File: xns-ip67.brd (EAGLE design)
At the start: 65.3 x 129.3 mm, 119 parts, among them J1 DCJ0202

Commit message: Rev 0
First Version without routing
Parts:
- removed SV1: (no value), con-lstb:MA03-1
- added 5.5V, PAD115, PAD116: WIREPAD1,6/0,9, wirepad:1,6/0,9
- added JP1, JP10, JP11, JP12, JP13, JP14, JP15, JP16, JP17, JP18, JP19, JP2, JP20, JP21, JP22, JP23, JP24, JP25, JP26, JP27, JP28, JP29, JP3, JP30, JP35, JP36, JP4, JP5, JP6, JP7, JP8, JP9: (no value), adafruit:1X08-CLEANBIG
- added JP31, JP32, JP33, JP34: (no value), microbuilder:1X12_ROUND
- added PROG: (no value), con-lstb:MA03-1
- added U1: (no value), SparkFun-PowerIC:SOT23-5
- added X2: (no value), microbuilder:4UCONN_20329
- moved PAD16 80.2 mm to (72.4, 21.6)
- moved PAD22 78.5 mm to (69.8, 29.2)
- moved PAD20 78.5 mm to (69.8, 31.8)
- moved PAD19 78.5 mm to (72.4, 31.8)
- moved PAD18 78.5 mm to (72.4, 29.2)
- moved PAD17 78.5 mm to (72.4, 26.7)
- moved PAD9 78.4 mm to (69.8, 47.0)
- moved PAD7 78.4 mm to (69.8, 44.5)
- moved PAD8 78.4 mm to (69.8, 34.3)
- moved PAD11 78.4 mm to (69.8, 41.9)
- moved PAD12 78.4 mm to (69.8, 39.4)
- moved PAD10 78.4 mm to (69.8, 36.8)
- moved PAD6 78.4 mm to (72.4, 47.0)
- moved PAD5 78.4 mm to (72.4, 44.5)
- moved PAD4 78.4 mm to (72.4, 41.9)
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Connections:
- new net N$23: JP3.1, JP3.2, JP3.3, JP3.4, JP3.5, JP3.6, JP3.7, JP3.8
- new net N$24: JP4.1, JP4.2, JP4.3, JP4.4, JP4.5, JP4.6, JP4.7, JP4.8
- new net N$25: JP5.1, JP5.2, JP5.3, JP5.4, JP5.5, JP5.6, JP5.7, JP5.8
- new net N$26: JP6.1, JP6.2, JP6.3, JP6.4, JP6.5, JP6.6, JP6.7, JP6.8
- new net N$27: JP7.1, JP7.2, JP7.3, JP7.4, JP7.5, JP7.6, JP7.7, JP7.8
- new net N$28: JP8.1, JP8.2, JP8.3, JP8.4, JP8.5, JP8.6, JP8.7, JP8.8
- new net N$29: JP9.1, JP9.2, JP9.3, JP9.4, JP9.5, JP9.6, JP9.7, JP9.8
- new net N$30: JP10.1, JP10.2, JP10.3, JP10.4, JP10.5, JP10.6, JP10.7, JP10.8
- new net N$31: JP11.1, JP11.2, JP11.3, JP11.4, JP11.5, JP11.6, JP11.7, JP11.8
- new net N$32: JP12.1, JP12.2, JP12.3, JP12.4, JP12.5, JP12.6, JP12.7, JP12.8
- new net N$33: JP13.1, JP13.2, JP13.3, JP13.4, JP13.5, JP13.6, JP13.7, JP13.8
- new net N$34: JP14.1, JP14.2, JP14.3, JP14.4, JP14.5, JP14.6, JP14.7, JP14.8
- new net N$35: JP15.1, JP15.2, JP15.3, JP15.4, JP15.5, JP15.6, JP15.7, JP15.8
- new net N$36: JP30.1, JP30.2, JP30.3, JP30.4, JP30.5, JP30.6, JP30.7, JP30.8
- new net N$37: JP29.1, JP29.2, JP29.3, JP29.4, JP29.5, JP29.6, JP29.7, JP29.8
- new net N$38: JP28.1, JP28.2, JP28.3, JP28.4, JP28.5, JP28.6, JP28.7, JP28.8
- new net N$39: JP27.1, JP27.2, JP27.3, JP27.4, JP27.5, JP27.6, JP27.7, JP27.8
- new net N$40: JP26.1, JP26.2, JP26.3, JP26.4, JP26.5, JP26.6, JP26.7, JP26.8
- new net N$41: JP25.1, JP25.2, JP25.3, JP25.4, JP25.5, JP25.6, JP25.7, JP25.8
- new net N$42: JP24.1, JP24.2, JP24.3, JP24.4, JP24.5, JP24.6, JP24.7, JP24.8
- new net N$43: JP22.1, JP22.2, JP22.3, JP22.4, JP22.5, JP22.6, JP22.7, JP22.8
- new net N$44: JP21.1, JP21.2, JP21.3, JP21.4, JP21.5, JP21.6, JP21.7, JP21.8
- new net N$45: JP20.1, JP20.2, JP20.3, JP20.4, JP20.5, JP20.6, JP20.7, JP20.8
- new net N$46: JP19.1, JP19.2, JP19.3, JP19.4, JP19.5, JP19.6, JP19.7, JP19.8
- new net N$47: JP18.1, JP18.2, JP18.3, JP18.4, JP18.5, JP18.6, JP18.7, JP18.8
- new net N$48: JP17.1, JP17.2, JP17.3, JP17.4, JP17.5, JP17.6, JP17.7, JP17.8
- new net N$49: JP16.1, JP16.2, JP16.3, JP16.4, JP16.5, JP16.6, JP16.7, JP16.8
- new net N$50: JP35.1, JP35.2, JP35.3, JP35.4, JP35.5, JP35.6, JP35.7, JP35.8
- new net N$51: JP36.1, JP36.2, JP36.3, JP36.4, JP36.5, JP36.6, JP36.7, JP36.8
- net GND: now also JP31.1, JP31.10, JP31.11, JP31.12, JP31.2, JP31.3, JP31.4, JP31.5, JP31.6, JP31.7, JP31.8, JP31.9, JP32.1, JP32.10, JP32.11, JP32.12, JP32.2, JP32.3, JP32.4, JP32.5, JP32.6, JP32.7, JP32.8, JP32.9, MDL1.9, PAD107.1, PAD108.1, PAD109.1, PAD110.1, PAD111.1, PAD25.1, PAD26.1, PAD39.1, PAD40.1, PROG.1, U1.2, X1.2, X2.BASE@1, X2.BASE@2, X2.GND, X2.SPRT@1, X2.SPRT@2, X2.SPRT@3, X2.SPRT@4
- net N$14: now also MDL1.22
- net N$15: now also MDL1.10
- net N$16: now also MDL1.11
- net N$17: now also MDL1.12
- net N$18: now also MDL1.13
- net N$19: now also MDL1.14
- net N$20: now also MDL1.16, PROG.3; no longer PAD103.1, PAD104.1, PAD105.1, PAD106.1
- net N$21: now also JP1.1, JP1.2, JP1.3, JP1.4, JP1.5, JP1.6, JP1.7, JP1.8; no longer PAD107.1, PAD108.1, PAD109.1, PAD110.1
- net N$22: now also JP2.1, JP2.2, JP2.3, JP2.4, JP2.5, JP2.6, JP2.7, JP2.8; no longer PAD111.1, PAD112.1, PAD113.1, PAD114.1
- net N$4: now also MDL1.15, PROG.2; no longer MDL1.8, PAD39.1, PAD40.1, PAD41.1, PAD42.1
- net VCC: now also 5.5V.1, U1.1, U1.3, X1.1, X2.VBUS
- net VDD: now also JP33.1, JP33.10, JP33.11, JP33.12, JP33.2, JP33.3, JP33.4, JP33.5, JP33.6, JP33.7, JP33.8, JP33.9, JP34.1, JP34.10, JP34.11, JP34.12, JP34.2, JP34.3, JP34.4, JP34.5, JP34.6, JP34.7, JP34.8, JP34.9, MDL1.8, PAD103.1, PAD104.1, PAD105.1, PAD106.1, PAD112.1, PAD113.1, PAD114.1, PAD115.1, PAD116.1, PAD41.1, PAD42.1, U1.5; no longer PAD25.1, PAD26.1
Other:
- board text added: "3.3V"
- board text added: "GND"
- board text added: "RX"
- board text added: "TX"

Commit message: Rev 0 Autoroute
Rev 0 with Autoroute
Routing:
- net VDD: track 0.00 -> 277.9 mm, vias 0 -> 1
- net VCC: track 0.00 -> 68.2 mm
- net N$12: track 0.00 -> 21.8 mm
- net N$1: track 0.00 -> 21.5 mm
- net N$51: track 0.00 -> 19.7 mm
- net N$47: track 0.00 -> 19.7 mm
- net N$44: track 0.00 -> 19.7 mm
- net N$39: track 0.00 -> 19.7 mm
- net N$36: track 0.00 -> 19.7 mm
- net N$50: track 0.00 -> 19.7 mm
- net N$33: track 0.00 -> 19.7 mm
- net N$30: track 0.00 -> 19.7 mm
- net N$24: track 0.00 -> 19.7 mm
- net N$21: track 0.00 -> 19.7 mm
- net N$42: track 0.00 -> 19.7 mm
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- added copper zone on layer 1, net GND
- added copper zone on layer 16, net GND
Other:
- board text added: "xns-ip67-rev-0"
- board text added: "xnsense.no"

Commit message: New route
reroute
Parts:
- moved JP31 1.27 mm to (15.9, 86.4)
- moved JP34 1.27 mm to (18.4, 86.4)
- moved JP1 0.63 mm to (31.8, 100.3)
- moved JP10 0.63 mm to (31.8, 77.5)
- moved JP11 0.63 mm to (31.8, 74.9)
- moved JP12 0.63 mm to (31.8, 72.4)
- moved JP13 0.63 mm to (31.8, 69.8)
- moved JP14 0.63 mm to (31.8, 67.3)
- moved JP15 0.63 mm to (31.8, 64.8)
- moved JP16 0.63 mm to (54.6, 64.8)
- moved JP17 0.63 mm to (54.6, 67.3)
- moved JP18 0.63 mm to (54.6, 69.8)
- moved JP19 0.63 mm to (54.6, 72.4)
- moved JP2 0.63 mm to (31.8, 97.8)
- moved JP20 0.63 mm to (54.6, 74.9)
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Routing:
- net VDD: track 277.9 -> 271.4 mm
- net VCC: track 68.2 -> 68.9 mm

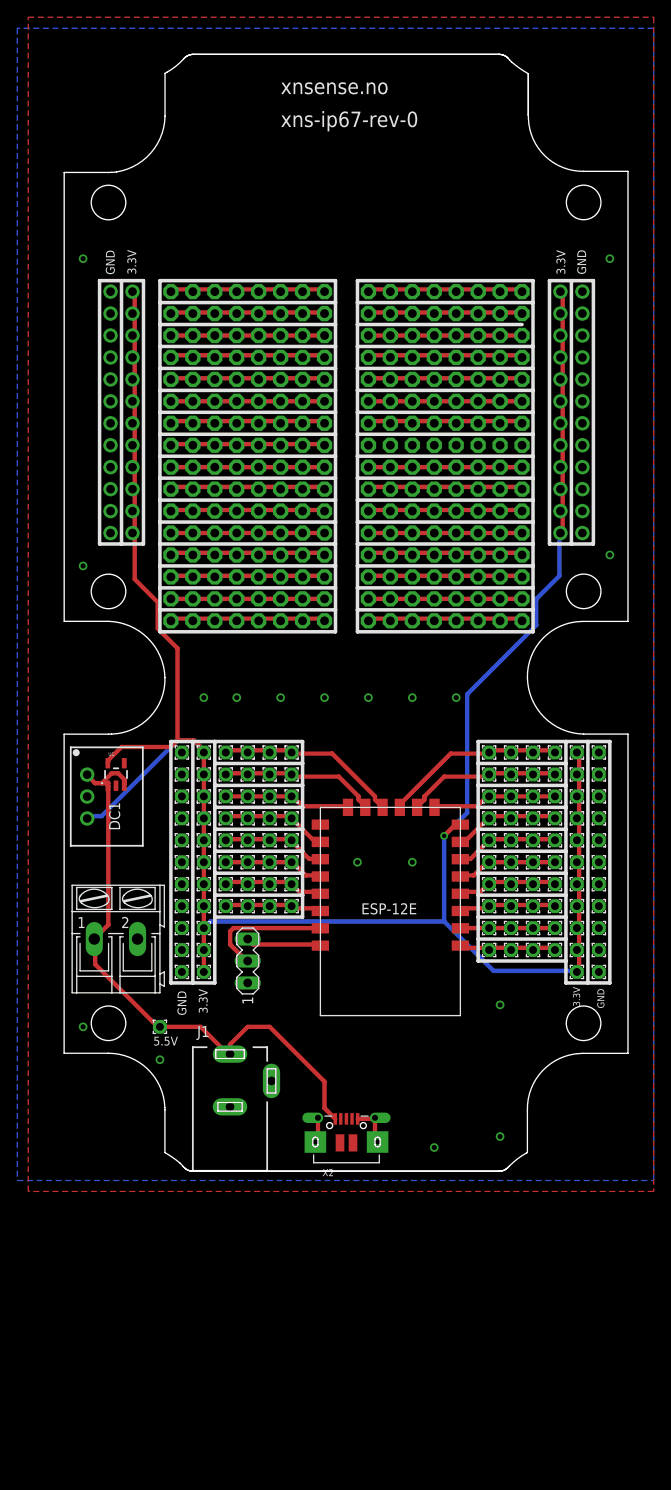
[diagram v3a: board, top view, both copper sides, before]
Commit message: Updated design
Added more wire pads on side of ESP
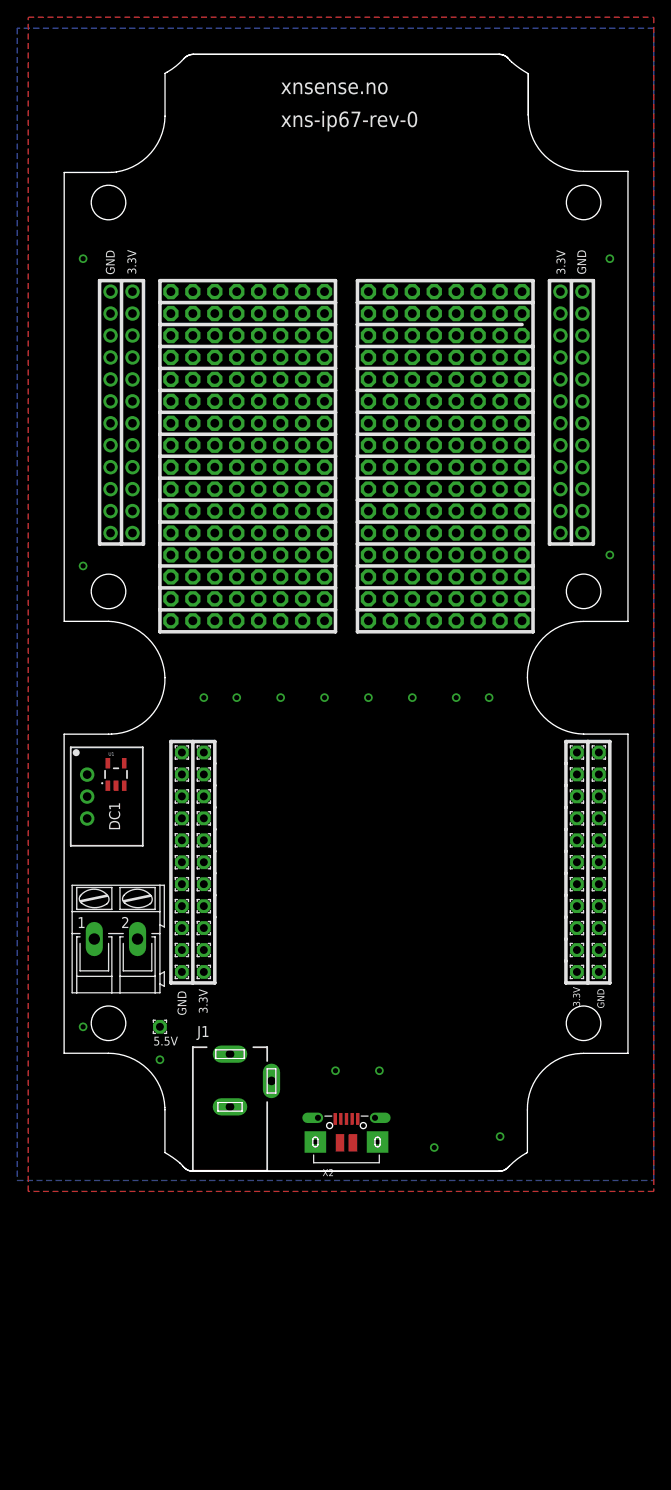
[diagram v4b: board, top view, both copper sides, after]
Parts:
- removed MDL1: (no value), ESP8266-ESP12E:ESP8266-ESP12E
- removed PAD100, PAD101, PAD102, PAD27, PAD28, PAD29, PAD30, PAD31, PAD32, PAD33, PAD34, PAD35, PAD36, PAD37, PAD38, PAD43, PAD44, PAD45, PAD46, PAD47, PAD48, PAD49, PAD50, PAD51, PAD52, PAD53, PAD54, PAD55, PAD56, PAD57, PAD58, PAD59, PAD60, PAD61, PAD62, PAD63, PAD64, PAD65, PAD66, PAD67, PAD68, PAD69, PAD70, PAD71, PAD72, PAD73, PAD74, PAD75, PAD76, PAD77, PAD78, PAD79, PAD80, PAD81, PAD82, PAD83, PAD84, PAD85, PAD86, PAD87, PAD88, PAD89, PAD90, PAD91, PAD92, PAD93, PAD94, PAD95, PAD96, PAD97, PAD98, PAD99: WIREPAD1,6/0,9, wirepad:1,6/0,9
- removed PROG: (no value), con-lstb:MA03-1
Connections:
- removed net N$1: MDL1.19, PAD27.1, PAD28.1, PAD29.1, PAD30.1
- removed net N$10: MDL1.2, PAD63.1, PAD64.1, PAD65.1, PAD66.1
- removed net N$11: MDL1.1, PAD67.1, PAD68.1, PAD69.1, PAD70.1
- removed net N$12: MDL1.20, PAD71.1, PAD72.1, PAD73.1, PAD74.1
- removed net N$13: MDL1.21, PAD75.1, PAD76.1, PAD77.1, PAD78.1
- removed net N$14: MDL1.22, PAD79.1, PAD80.1, PAD81.1, PAD82.1
- removed net N$15: MDL1.10, PAD83.1, PAD84.1, PAD85.1, PAD86.1
- removed net N$16: MDL1.11, PAD87.1, PAD88.1, PAD89.1, PAD90.1
- removed net N$17: MDL1.12, PAD91.1, PAD92.1, PAD93.1, PAD94.1
- removed net N$18: MDL1.13, PAD95.1, PAD96.1, PAD97.1, PAD98.1
- removed net N$19: MDL1.14, PAD100.1, PAD101.1, PAD102.1, PAD99.1
- removed net N$2: MDL1.18, PAD31.1, PAD32.1, PAD33.1, PAD34.1
- removed net N$20: MDL1.16, PROG.3
- removed net N$3: MDL1.17, PAD35.1, PAD36.1, PAD37.1, PAD38.1
- removed net N$4: MDL1.15, PROG.2
- removed net N$5: MDL1.7, PAD43.1, PAD44.1, PAD45.1, PAD46.1
- removed net N$6: MDL1.6, PAD47.1, PAD48.1, PAD49.1, PAD50.1
- removed net N$7: MDL1.5, PAD51.1, PAD52.1, PAD53.1, PAD54.1
- removed net N$8: MDL1.4, PAD55.1, PAD56.1, PAD57.1, PAD58.1
- removed net N$9: MDL1.3, PAD59.1, PAD60.1, PAD61.1, PAD62.1
- net GND: no longer MDL1.9, PROG.1
- net VDD: no longer MDL1.8
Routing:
- net VDD: track 271.4 -> 0.00 mm, vias 1 -> 0
- net VCC: track 68.9 -> 0.00 mm
- net N$12: track 21.8 -> 0.00 mm
- net N$1: track 21.5 -> 0.00 mm
- net N$50: track 19.7 -> 0.00 mm
- net N$33: track 19.7 -> 0.00 mm
- net N$30: track 19.7 -> 0.00 mm
- net N$24: track 19.7 -> 0.00 mm
- net N$21: track 19.7 -> 0.00 mm
- net N$51: track 19.7 -> 0.00 mm
- net N$47: track 19.7 -> 0.00 mm
- net N$44: track 19.7 -> 0.00 mm
- net N$39: track 19.7 -> 0.00 mm
- net N$36: track 19.7 -> 0.00 mm
- net N$42: track 19.7 -> 0.00 mm
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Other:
- board text removed: "RX"
- board text removed: "TX"

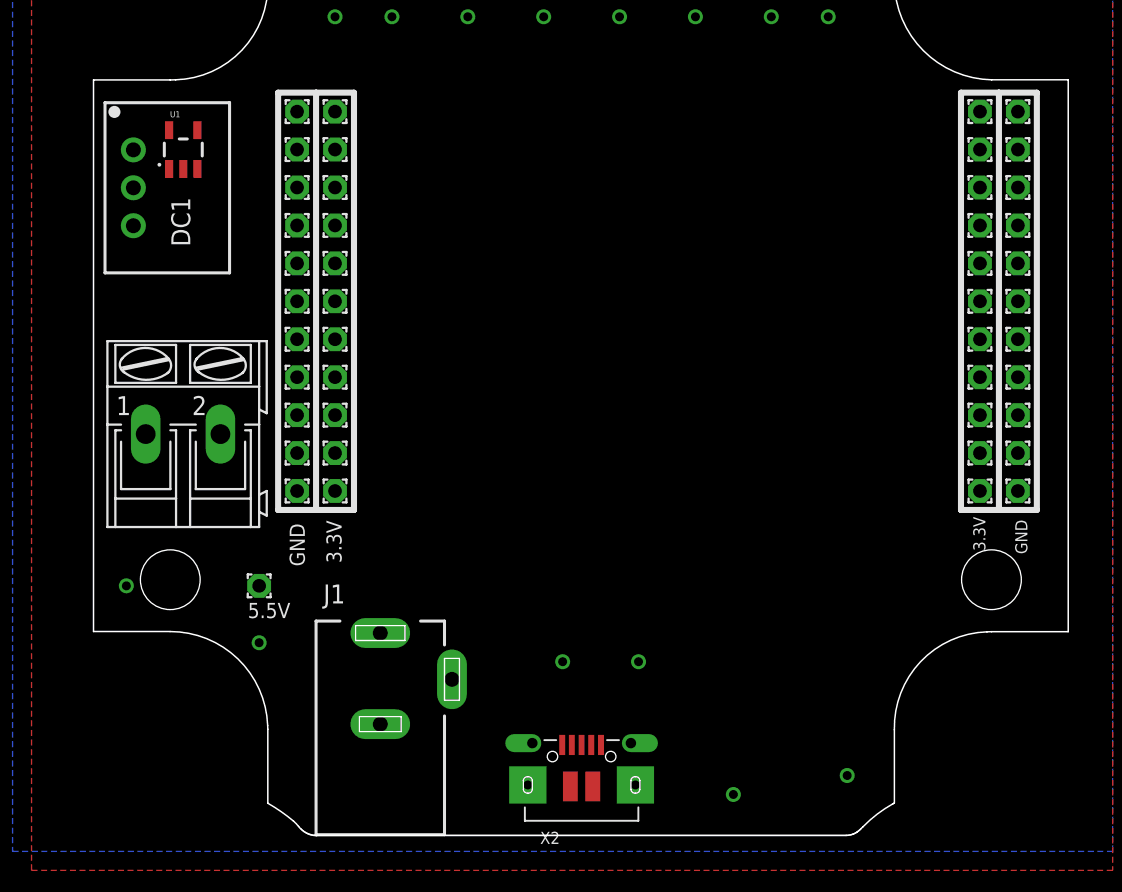
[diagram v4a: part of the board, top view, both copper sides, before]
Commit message: Version without esp8266
Simple version
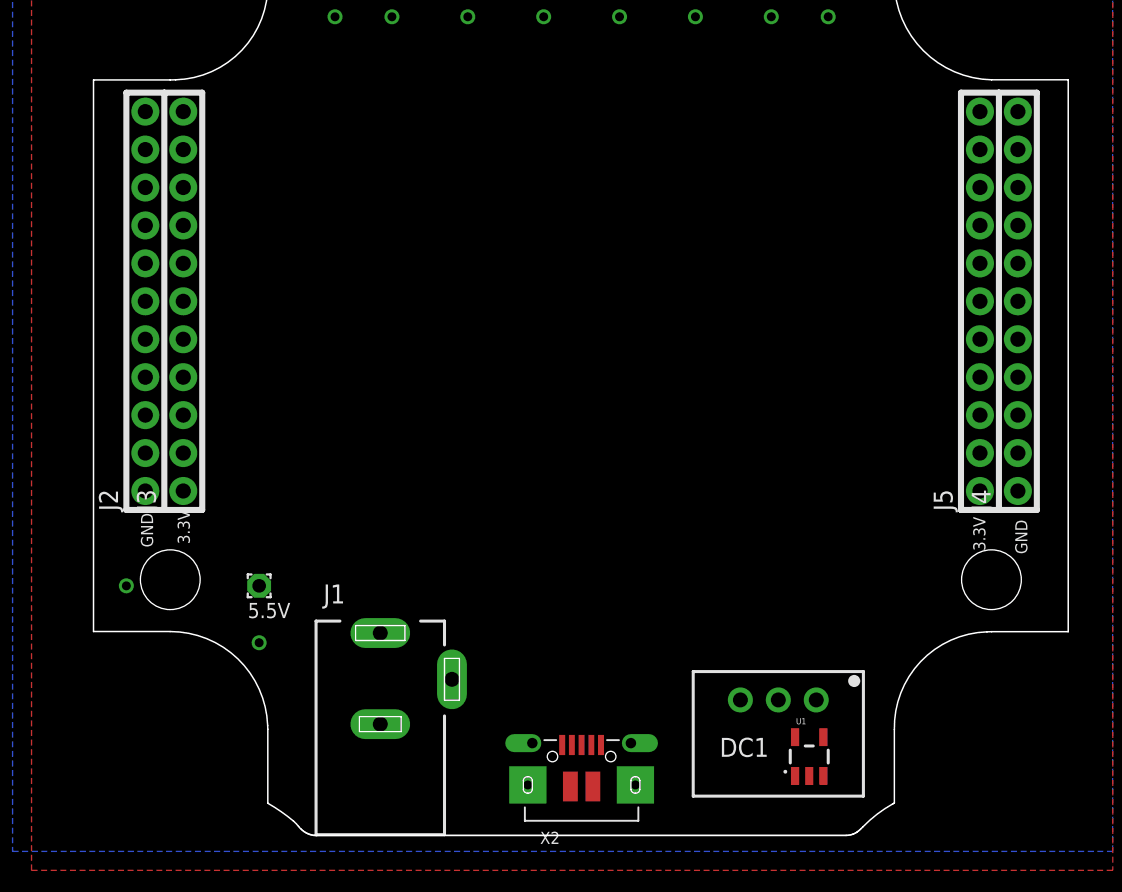
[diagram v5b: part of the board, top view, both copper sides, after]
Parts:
- removed PAD1, PAD10, PAD103, PAD104, PAD105, PAD106, PAD107, PAD108, PAD109, PAD11, PAD110, PAD111, PAD112, PAD113, PAD114, PAD115, PAD116, PAD12, PAD13, PAD14, PAD15, PAD16, PAD17, PAD18, PAD19, PAD2, PAD20, PAD21, PAD22, PAD23, PAD24, PAD25, PAD26, PAD3, PAD39, PAD4, PAD40, PAD41, PAD42, PAD5, PAD6, PAD7, PAD8, PAD9: WIREPAD1,6/0,9, wirepad:1,6/0,9
- removed X1: (no value), con-ptr500:AK300/2
- added J2, J3, J4, J5: (no value), SparkFun-Connectors:1X11_NO_SILK
- moved U1 58.4 mm to (58.4, 3.81)
- moved DC1 55.1 mm to (56.4, 7.60), turned to 180 degrees
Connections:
- net GND: now also J2.1, J2.10, J2.11, J2.2, J2.3, J2.4, J2.5, J2.6, J2.7, J2.8, J2.9, J4.1, J4.10, J4.11, J4.2, J4.3, J4.4, J4.5, J4.6, J4.7, J4.8, J4.9; no longer PAD1.1, PAD107.1, PAD108.1, PAD109.1, PAD110.1, PAD111.1, PAD13.1, PAD14.1, PAD15.1, PAD16.1, PAD17.1, PAD18.1, PAD19.1, PAD2.1, PAD25.1, PAD26.1, PAD3.1, PAD39.1, PAD4.1, PAD40.1, PAD5.1, PAD6.1, X1.2
- net VCC: no longer X1.1
- net VDD: now also J3.1, J3.10, J3.11, J3.2, J3.3, J3.4, J3.5, J3.6, J3.7, J3.8, J3.9, J5.1, J5.10, J5.11, J5.2, J5.3, J5.4, J5.5, J5.6, J5.7, J5.8, J5.9; no longer PAD10.1, PAD103.1, PAD104.1, PAD105.1, PAD106.1, PAD11.1, PAD112.1, PAD113.1, PAD114.1, PAD115.1, PAD116.1, PAD12.1, PAD20.1, PAD21.1, PAD22.1, PAD23.1, PAD24.1, PAD41.1, PAD42.1, PAD7.1, PAD8.1, PAD9.1

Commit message: Routed and Gerb files
Routed and produced verb files
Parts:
- added J10, J11, J12, J13, J14, J15, J16, J17, J18, J19, J20, J21, J22, J23, J24, J25, J26, J27, J6, J7, J8, J9: (no value), SparkFun-Connectors:1X09_NO_SILK
- moved U1 8.98 mm to (59.7, 12.7), turned to 180 degrees
- moved X2 0.95 mm to (43.2, 2.86)
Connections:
- new net N$1: J6.1, J6.2, J6.3, J6.4, J6.5, J6.6, J6.7, J6.8, J6.9
- new net N$10: J15.1, J15.2, J15.3, J15.4, J15.5, J15.6, J15.7, J15.8, J15.9
- new net N$11: J16.1, J16.2, J16.3, J16.4, J16.5, J16.6, J16.7, J16.8, J16.9
- new net N$12: J17.1, J17.2, J17.3, J17.4, J17.5, J17.6, J17.7, J17.8, J17.9
- new net N$13: J18.1, J18.2, J18.3, J18.4, J18.5, J18.6, J18.7, J18.8, J18.9
- new net N$14: J19.1, J19.2, J19.3, J19.4, J19.5, J19.6, J19.7, J19.8, J19.9
- new net N$15: J20.1, J20.2, J20.3, J20.4, J20.5, J20.6, J20.7, J20.8, J20.9
- new net N$16: J21.1, J21.2, J21.3, J21.4, J21.5, J21.6, J21.7, J21.8, J21.9
- new net N$17: J22.1, J22.2, J22.3, J22.4, J22.5, J22.6, J22.7, J22.8, J22.9
- new net N$18: J23.1, J23.2, J23.3, J23.4, J23.5, J23.6, J23.7, J23.8, J23.9
- new net N$19: J24.1, J24.2, J24.3, J24.4, J24.5, J24.6, J24.7, J24.8, J24.9
- new net N$2: J7.1, J7.2, J7.3, J7.4, J7.5, J7.6, J7.7, J7.8, J7.9
- new net N$20: J25.1, J25.2, J25.3, J25.4, J25.5, J25.6, J25.7, J25.8, J25.9
- new net N$3: J8.1, J8.2, J8.3, J8.4, J8.5, J8.6, J8.7, J8.8, J8.9
- new net N$4: J9.1, J9.2, J9.3, J9.4, J9.5, J9.6, J9.7, J9.8, J9.9
- new net N$5: J10.1, J10.2, J10.3, J10.4, J10.5, J10.6, J10.7, J10.8, J10.9
- new net N$52: J26.1, J26.2, J26.3, J26.4, J26.5, J26.6, J26.7, J26.8, J26.9
- new net N$53: J27.1, J27.2, J27.3, J27.4, J27.5, J27.6, J27.7, J27.8, J27.9
- new net N$54: JP23.1, JP23.2, JP23.3, JP23.4, JP23.5, JP23.6, JP23.7, JP23.8
- new net N$6: J11.1, J11.2, J11.3, J11.4, J11.5, J11.6, J11.7, J11.8, J11.9
- new net N$7: J12.1, J12.2, J12.3, J12.4, J12.5, J12.6, J12.7, J12.8, J12.9
- new net N$8: J13.1, J13.2, J13.3, J13.4, J13.5, J13.6, J13.7, J13.8, J13.9
- new net N$9: J14.1, J14.2, J14.3, J14.4, J14.5, J14.6, J14.7, J14.8, J14.9
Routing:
- net VDD: track 0.00 -> 287.6 mm, vias 0 -> 3
- net VCC: track 0.00 -> 77.4 mm, vias 0 -> 1
- net N$4: track 0.00 -> 22.5 mm
- net N$10: track 0.00 -> 22.5 mm
- net N$7: track 0.00 -> 22.5 mm
- net N$15: track 0.00 -> 22.3 mm
- net N$52: track 0.00 -> 22.3 mm, vias 1 -> 0
- net N$18: track 0.00 -> 22.3 mm
- net N$5: track 0.00 -> 21.2 mm
- net N$8: track 0.00 -> 21.2 mm
- net N$11: track 0.00 -> 21.2 mm
- net N$2: track 0.00 -> 21.2 mm
- net N$16: track 0.00 -> 21.1 mm
- net N$53: track 0.00 -> 21.1 mm, vias 1 -> 0
- net N$19: track 0.00 -> 21.1 mm
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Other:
- board text added: "xns ip67 rev 1"
- board text removed: "xns-ip67-rev-0"
